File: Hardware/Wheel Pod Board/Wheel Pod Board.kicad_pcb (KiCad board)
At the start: 2 copper layers, 42 parts, among them J1 Conn_RJ-45, P1 UIM240XX_Stepper_Conn, P2 RS232, P3 ST_SWD_Connector, P4 RS485, P5 BATT, P6 SyRen Pwr, U1 STM32F401RCT6, X1 24MHz

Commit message: More parts on PCB
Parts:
- moved J1 275.7 mm to (238.6, 138.2)
- moved P5 241.7 mm to (200.2, 135.4)
- moved P6 227.7 mm to (174.6, 146.2)
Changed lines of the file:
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@@
   (general
     (links 78)
-    (no_connects 77)
+    (no_connects 78)
     (area 0 0 0 0)
     (thickness 1.6)
@@
   )
   (module Connect:RJ45_8 (layer F.Cu)
-    (at 0 0)
+    (at 238.6 138.2)
     (tags RJ45)
     (fp_text reference J1 (at 0.254 4.826) (layer F.SilkS)
@@
   )
   (module MAVRIC_footprints:1x2_SMD_header (layer F.Cu)
-    (at 0 0)
+    (at 200.2 135.4)
     (fp_text reference P5 (at 0 -4) (layer F.SilkS) hide
       (effects (font (size 1.5 1.5) (thickness 0.15)))
@@
   )
   (module MAVRIC_footprints:1x2_SMD_header (layer F.Cu)
-    (at 0 0)
+    (at 174.6 146.2)
     (fp_text reference P6 (at 0 -4) (layer F.SilkS) hide
       (effects (font (size 1.5 1.5) (thickness 0.15)))

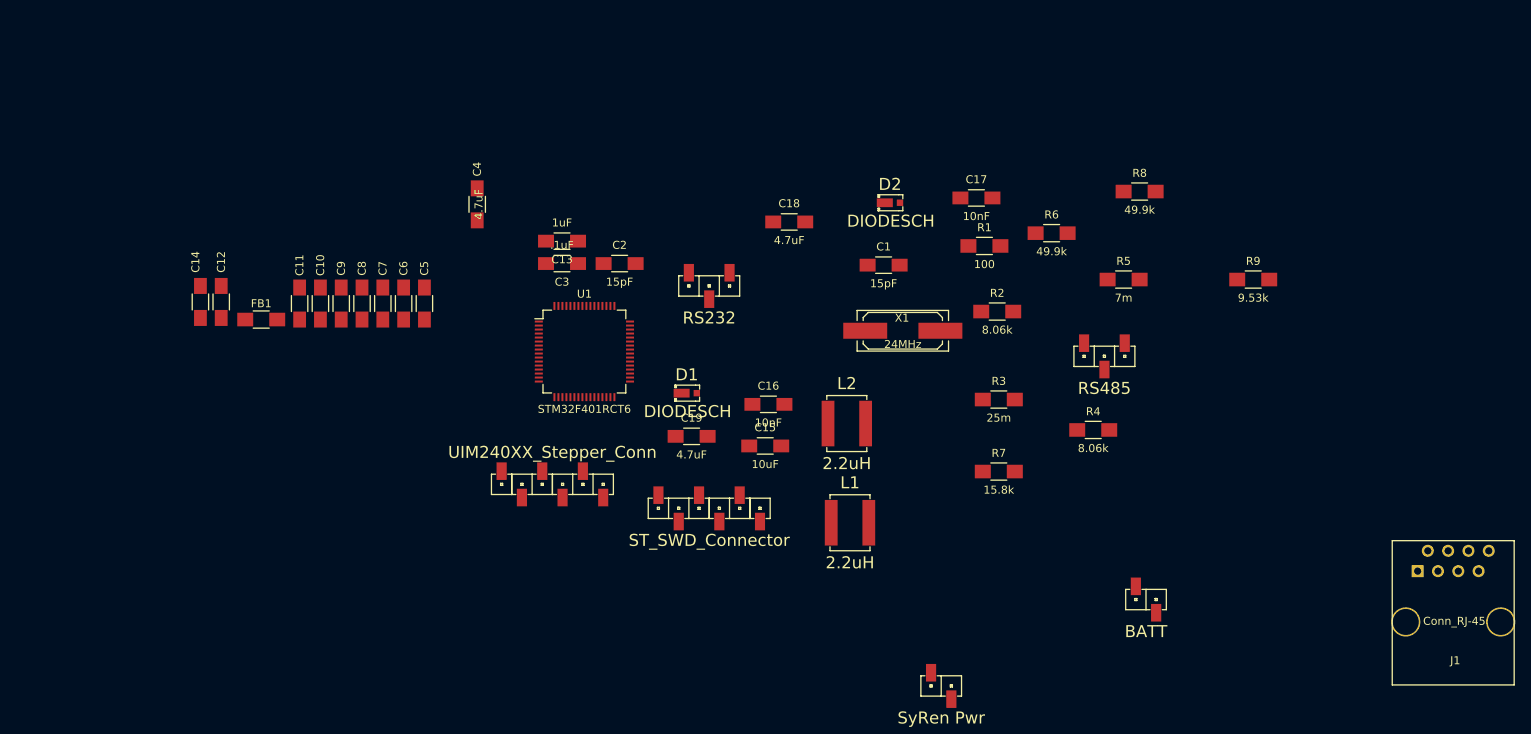
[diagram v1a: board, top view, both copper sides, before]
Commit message: Fix footprints, add RJ45 jack to pcb
Resolve #12, Resolve #5
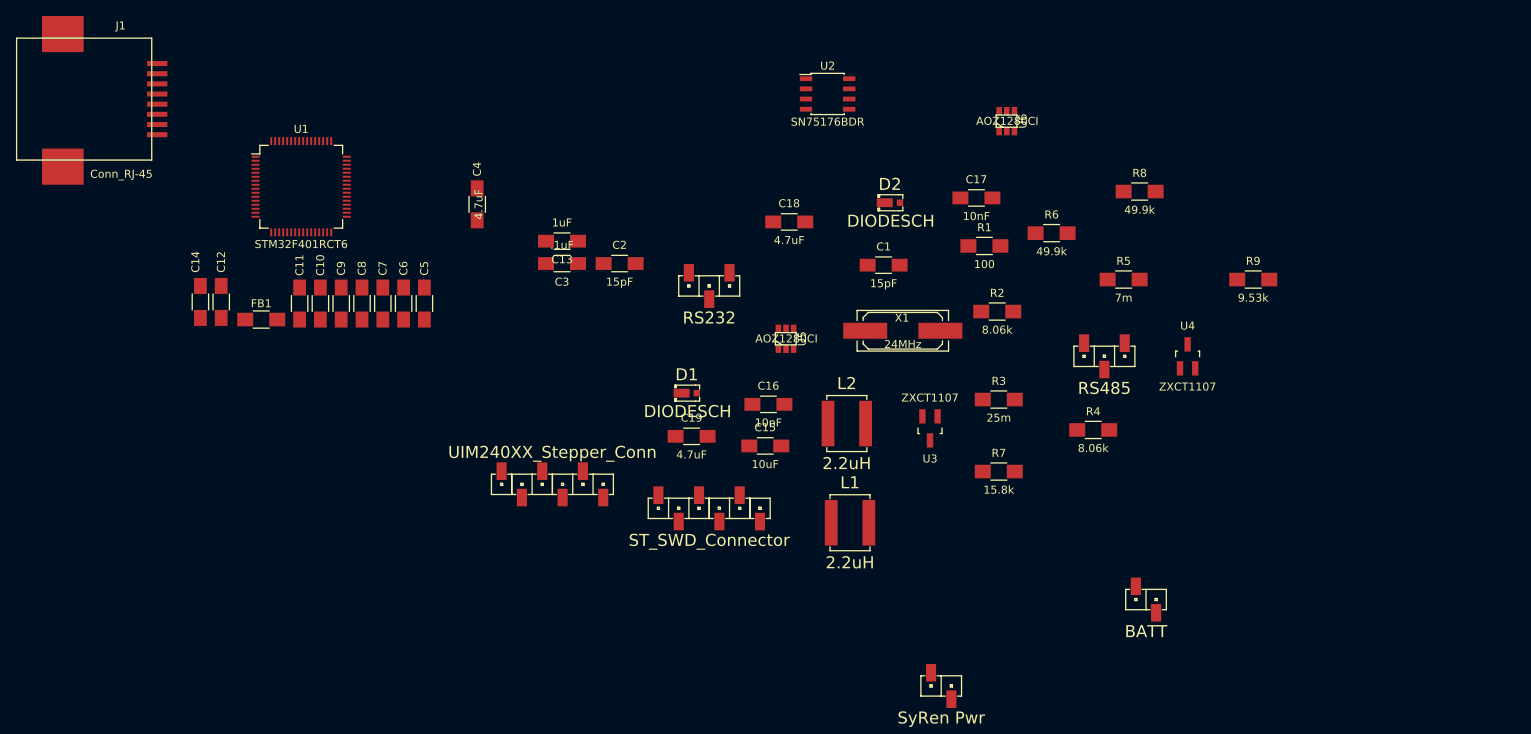
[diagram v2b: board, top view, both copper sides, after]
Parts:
- added U2: SN75176BDR, Housings_SOIC:SOIC-8_3.9x4.9mm_Pitch1.27mm, F.Cu at (160.4, 72.2)
- added U3: ZXCT1107, Housings_SOT-23_SOT-143_TSOT-6:SOT23_Handsoldering, F.Cu at (173.2, 114.0)
- added U4: ZXCT1107, Housings_SOT-23_SOT-143_TSOT-6:SOT23_Handsoldering, F.Cu at (205.4, 105.0)
- added U5: AOZ1280CI, Housings_SOT-23_SOT-143_TSOT-6:SOT-23-6, F.Cu at (155.2, 102.8)
- added U6: AOZ1280CI, Housings_SOT-23_SOT-143_TSOT-6:SOT-23-6, F.Cu at (182.8, 75.6)
- J1: footprint Connect:RJ45_8 -> MAVRIC_footprints:Molex_RJ45_0437438101
- moved J1 176.4 mm to (76.6, 68.4), turned to 270 degrees
- moved U1 41.0 mm to (94.6, 83.8)
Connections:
- J1 pad 7: Net-(J1-Pad7) -> GND
- J1 pad 8: Net-(J1-Pad8) -> GND
- R1 pad 1: /485_A -> Net-(J1-Pad5)
- R1 pad 2: /485_B -> Net-(J1-Pad4)

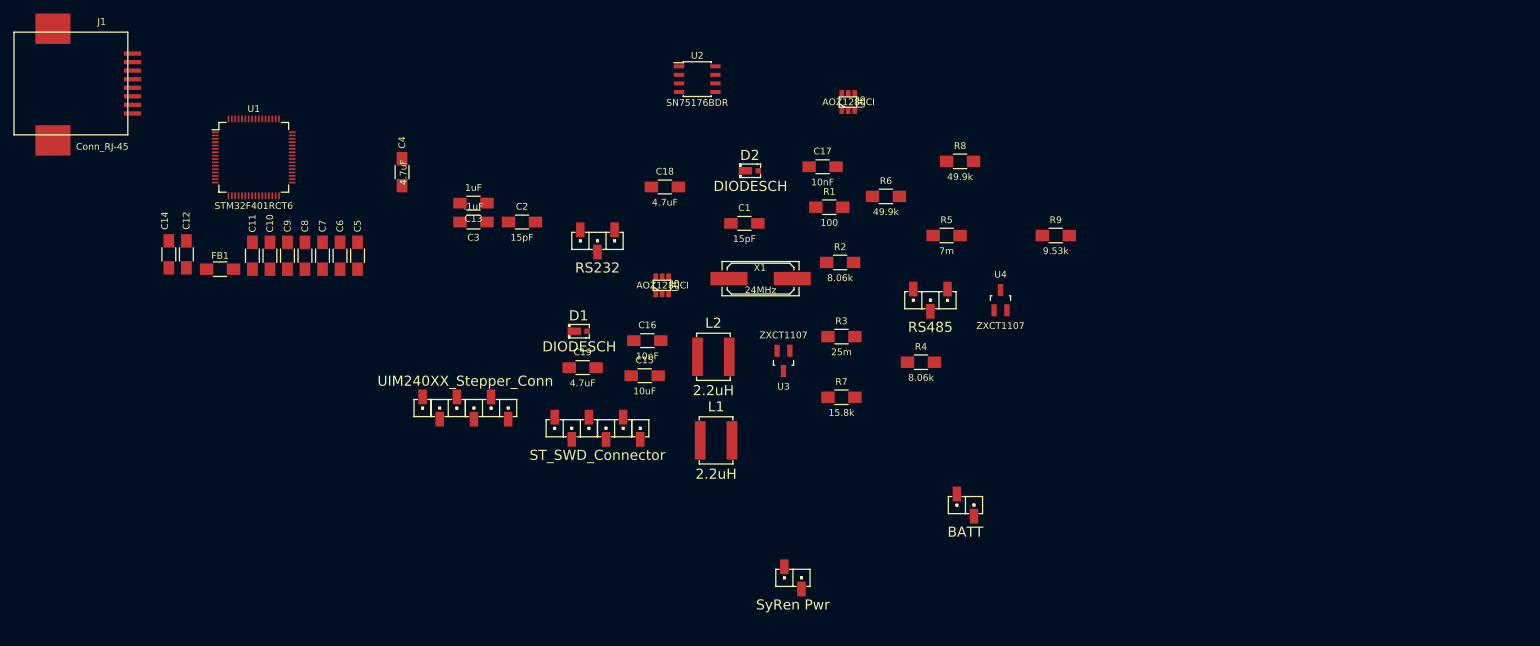
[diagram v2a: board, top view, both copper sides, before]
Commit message: Reroute 3V3 and 5V through cat5, remove regs
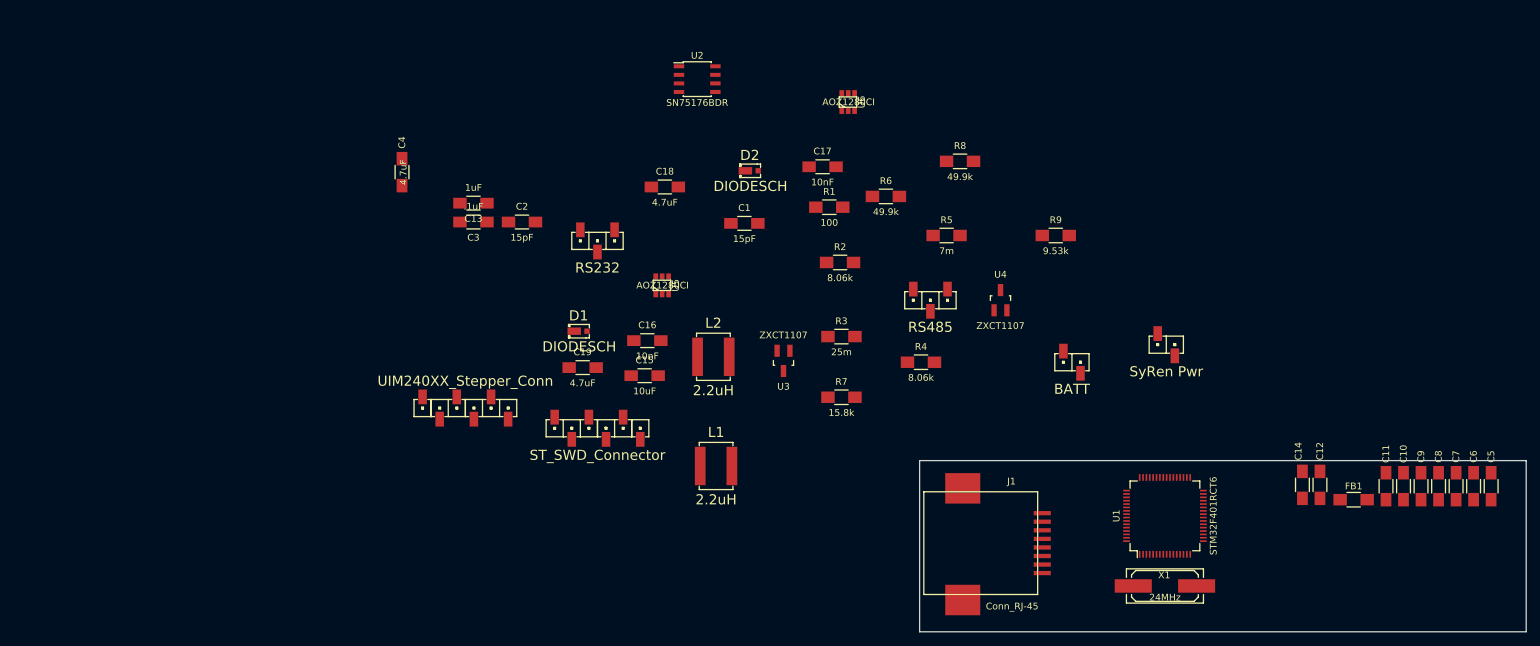
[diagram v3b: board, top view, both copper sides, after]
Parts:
- moved C11 171.6 mm to (262.6, 132.6)
- moved C12 171.6 mm to (252.8, 132.4)
- moved C6 171.6 mm to (275.6, 132.6)
- moved C9 171.6 mm to (267.8, 132.6)
- moved FB1 171.6 mm to (257.8, 134.6)
- moved C10 171.6 mm to (265.2, 132.6)
- moved C14 171.6 mm to (250.2, 132.4)
- moved C5 171.6 mm to (278.2, 132.6)
- moved C7 171.6 mm to (273.0, 132.6)
- moved C8 171.6 mm to (270.4, 132.6)
- moved J1 151.2 mm to (211.6, 136.6)
- moved U1 145.3 mm to (229.8, 137.0), turned to 90 degrees
- moved X1 75.4 mm to (229.8, 147.4)
- moved P6 65.3 mm to (230.0, 111.6)
- moved P5 26.4 mm to (216.0, 114.2)
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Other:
- board outline added: 90 x 25.4 mm

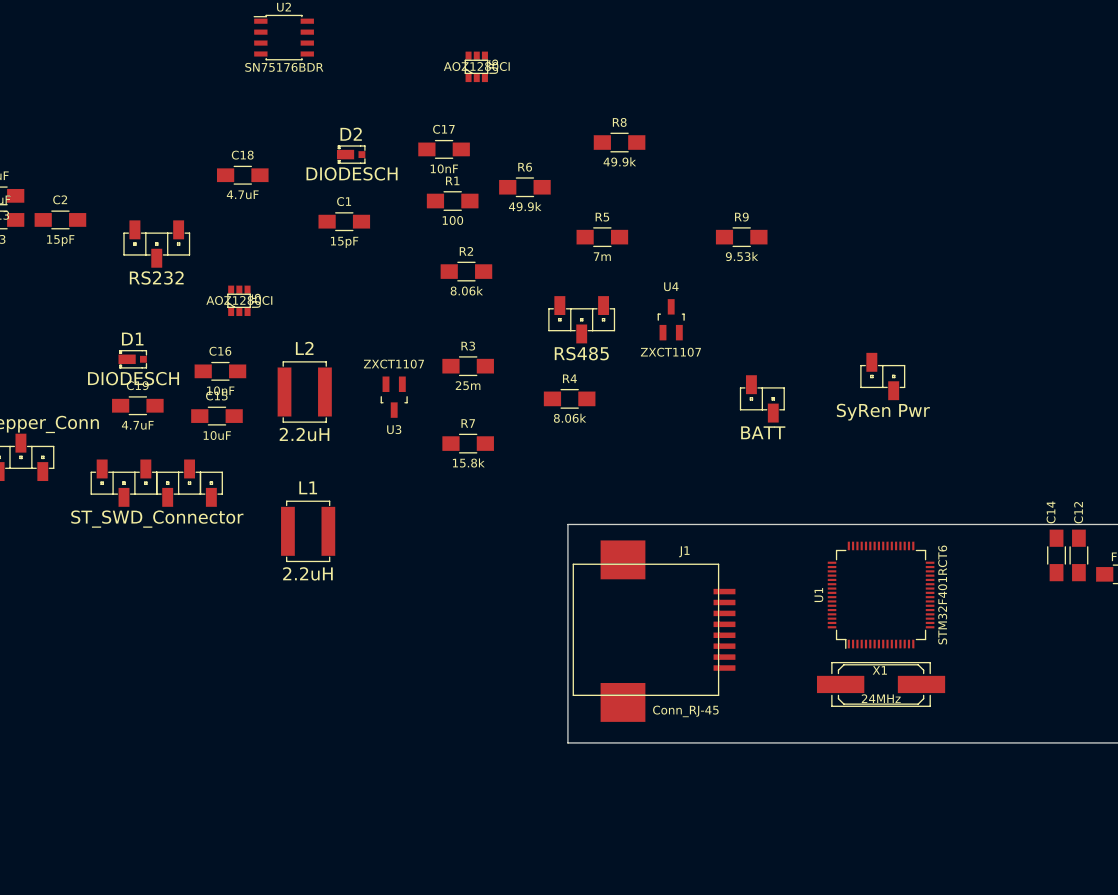
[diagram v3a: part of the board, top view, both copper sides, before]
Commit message: Update cube, make connections to microcontroller
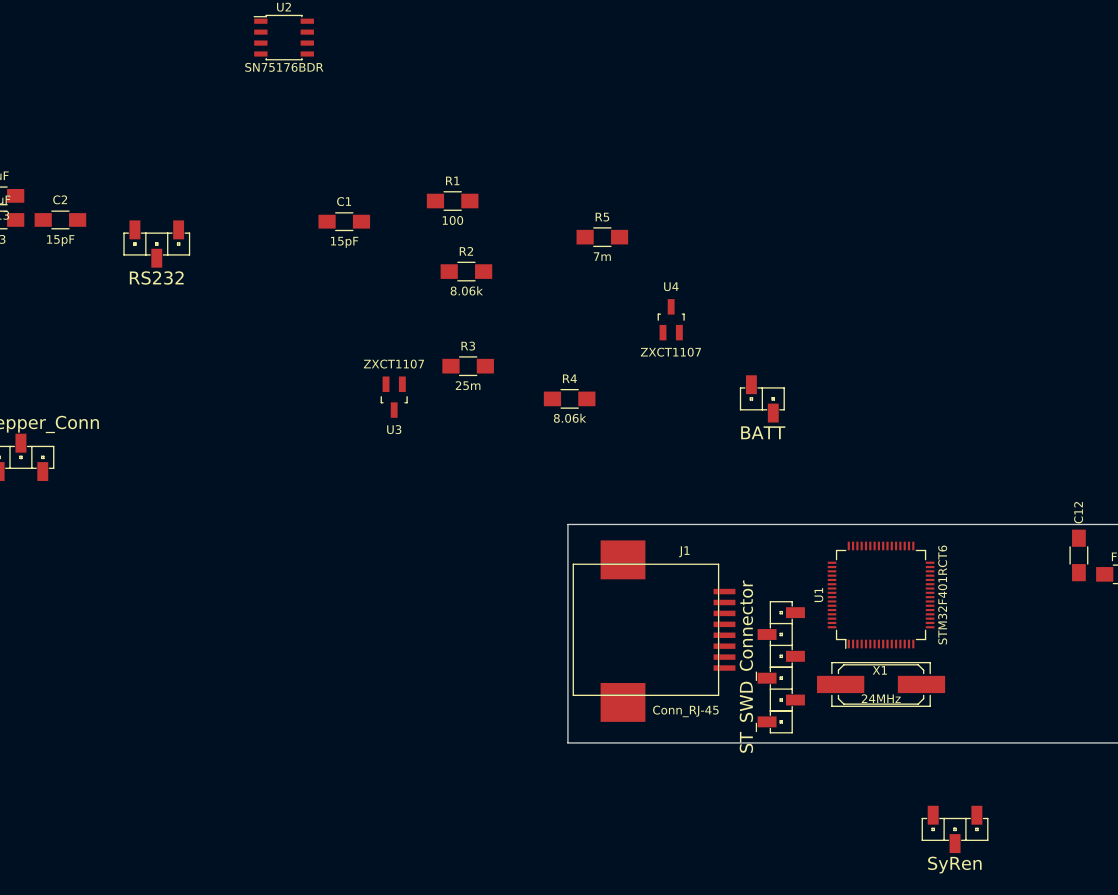
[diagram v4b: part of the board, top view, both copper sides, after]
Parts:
- removed C14, C15: 10uF, Capacitors_SMD:C_1206_HandSoldering
- removed C16, C17: 10nF, Capacitors_SMD:C_1206_HandSoldering
- removed C18, C19: 4.7uF, Capacitors_SMD:C_1206_HandSoldering
- removed D1, D2: DIODESCH, MAVRIC_footprints:Diode_MicroSMP
- removed L1, L2: 2.2uH, MAVRIC_footprints:Yuden_SMD_Power_Inductor_6060
- removed P6: SyRen Pwr, MAVRIC_footprints:1x2_SMD_header
- removed R6, R8: 49.9k, Resistors_SMD:R_1206_HandSoldering
- removed R7: 15.8k, Resistors_SMD:R_1206_HandSoldering
- removed R9: 9.53k, Resistors_SMD:R_1206_HandSoldering
- removed U5, U6: AOZ1280CI, Housings_SOT-23_SOT-143_TSOT-6:SOT-23-6
- P4: value RS485 -> SyRen
- moved P3 75.7 mm to (218.2, 145.4), turned to 270 degrees
- moved P4 73.4 mm to (238.4, 164.3)
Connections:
- J1 pad 3: Net-(J1-Pad3) -> +5V
- J1 pad 6: Net-(J1-Pad6) -> GND
- J1 pad 7: GND -> +3V3
- P4 pad 1: /485_B -> GND
- P4 pad 2: /485_A -> Net-(P4-Pad2)
- P4 pad 3: GND -> /USART2_TX
- R5 pad 2: Net-(P6-Pad2) -> Net-(P4-Pad2)
- U1 pad 14: Net-(U1-Pad14) -> /StepperCurrent
- U1 pad 15: Net-(U1-Pad15) -> /SyRenCurrent
- U1 pad 16: Net-(U1-Pad16) -> /USART2_TX
- U1 pad 34: Net-(U1-Pad34) -> /Step_Enable
- U1 pad 35: Net-(U1-Pad35) -> /Step_Direction
- U1 pad 41: Net-(U1-Pad41) -> /Step_Step
- U1 pad 46: Net-(U1-Pad46) -> /SWDIO
- U1 pad 49: Net-(U1-Pad49) -> /SWCLK
- U4 pad 3: Net-(P6-Pad2) -> Net-(P4-Pad2)
